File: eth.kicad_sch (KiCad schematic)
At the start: 44 parts, among them J5 Bus_RJ45_5-2337992-8, Q4 DTC014T_SOT-416, Q5 DTC014T_SOT-416, U30 DP83867CR_VQFN, Y6 Oscillator_25MHz_ESC_2016MV

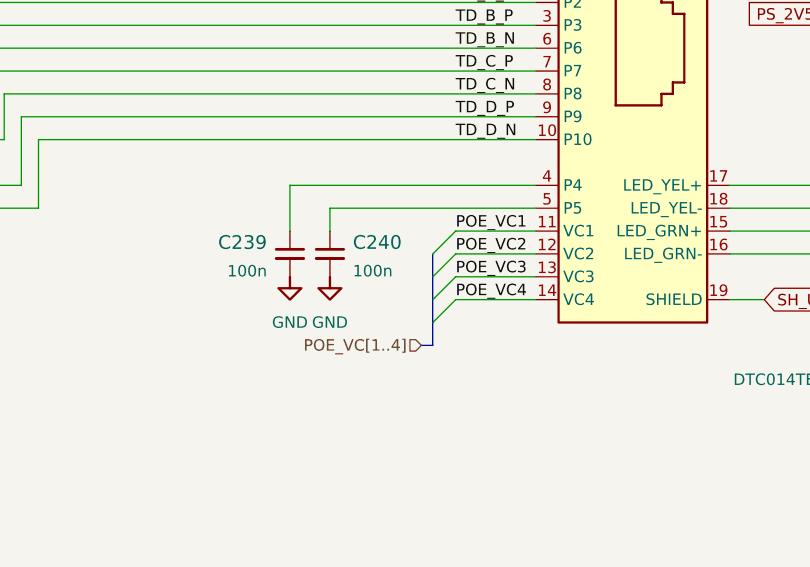
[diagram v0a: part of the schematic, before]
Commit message: removed PoE from schematic
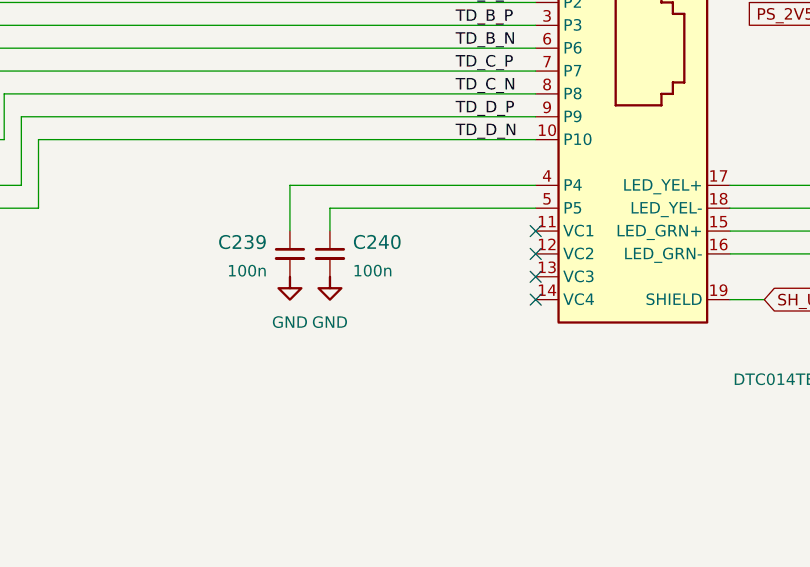
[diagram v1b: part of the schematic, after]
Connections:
- net POE_VC1: no longer names the net of J5.11 (VC1)
- net POE_VC2: no longer names the net of J5.12 (VC2)
- net POE_VC3: no longer names the net of J5.13 (VC3)
- net POE_VC4: no longer names the net of J5.14 (VC4)
- no-connect marks 9 -> 13
